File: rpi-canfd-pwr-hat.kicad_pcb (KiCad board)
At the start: 4 copper layers, 65 x 56 mm, 90 parts, among them J1 Conn_01x02, J2 Conn_01x04_Pin, J3 Raspberry_Pi, J4 Conn_01x02, J5 Conn_01x02, U1 XC6206P332MR, U10 SN74LV1T125DBV, U11 SN74LV1T125DBV, U12 SN74LV1T125DBV, U13 SN74LV1T125DBV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

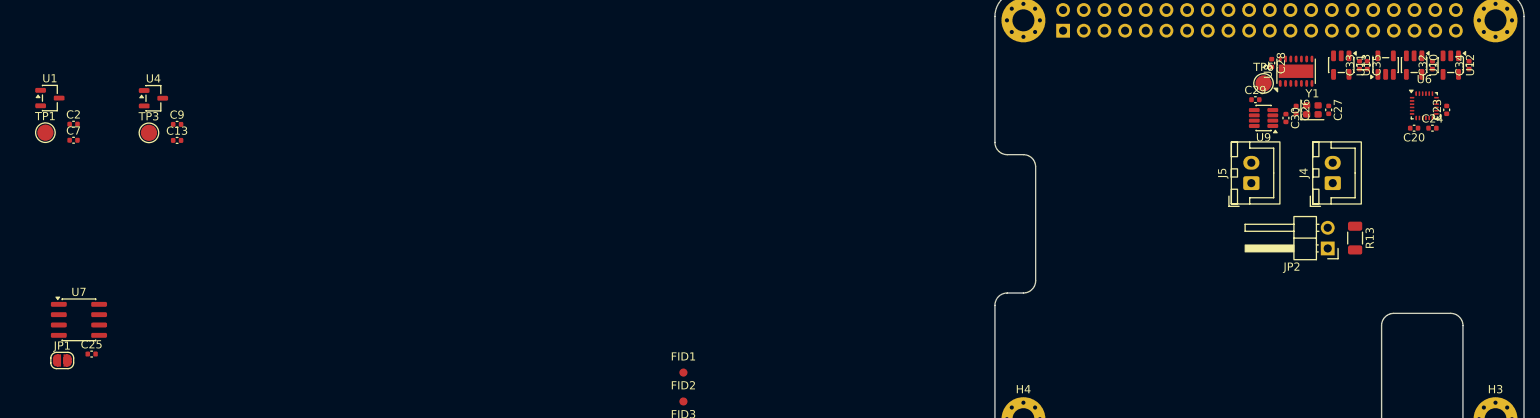
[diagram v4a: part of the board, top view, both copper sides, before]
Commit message: pcb: add eeprom routing
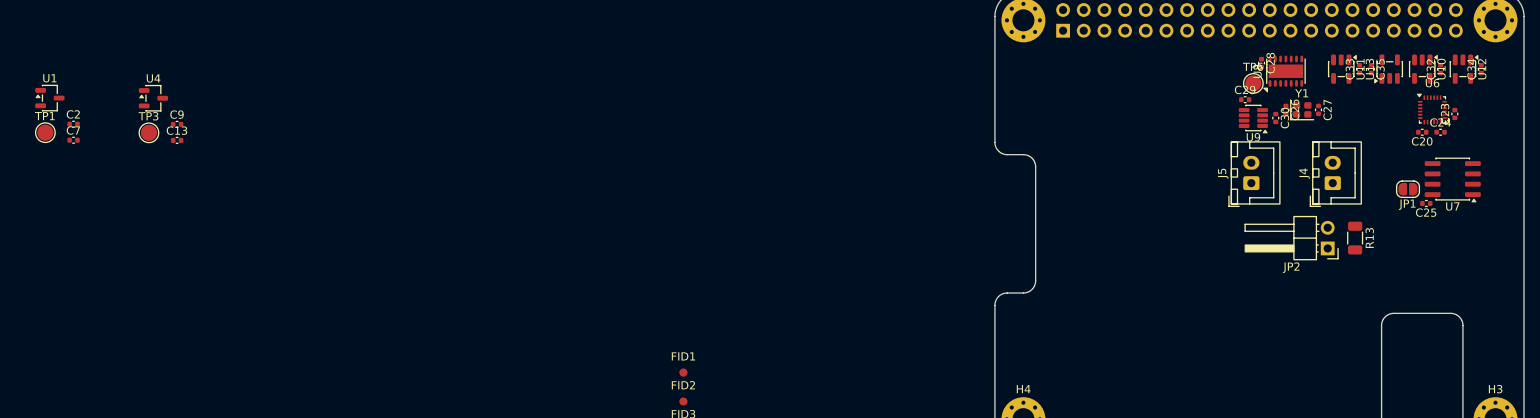
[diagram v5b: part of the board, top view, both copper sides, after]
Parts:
- moved U7 169.7 mm to (206.2, 93.0), turned to 180 degrees
- moved JP1 166.7 mm to (200.8, 94.2), turned to 180 degrees
- moved C25 165.0 mm to (203.0, 96.0), turned to 180 degrees
- moved C34 1.58 mm to (209.8, 79.5)
- moved U12 1.58 mm to (207.5, 79.5)
- moved C26 1.25 mm to (185.8, 84.5)
- moved C27 1.25 mm to (189.8, 84.5)
- moved C28 1.25 mm to (182.8, 78.8)
- moved C29 1.25 mm to (180.8, 83.2)
- moved C30 1.25 mm to (184.5, 85.5)
- moved TP6 1.25 mm to (181.8, 81.2)
- moved U8 1.25 mm to (185.8, 79.8)
- moved U9 1.25 mm to (181.8, 85.5)
- moved Y1 1.25 mm to (187.8, 84.5)
- moved C20 1.12 mm to (202.5, 87.2)
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
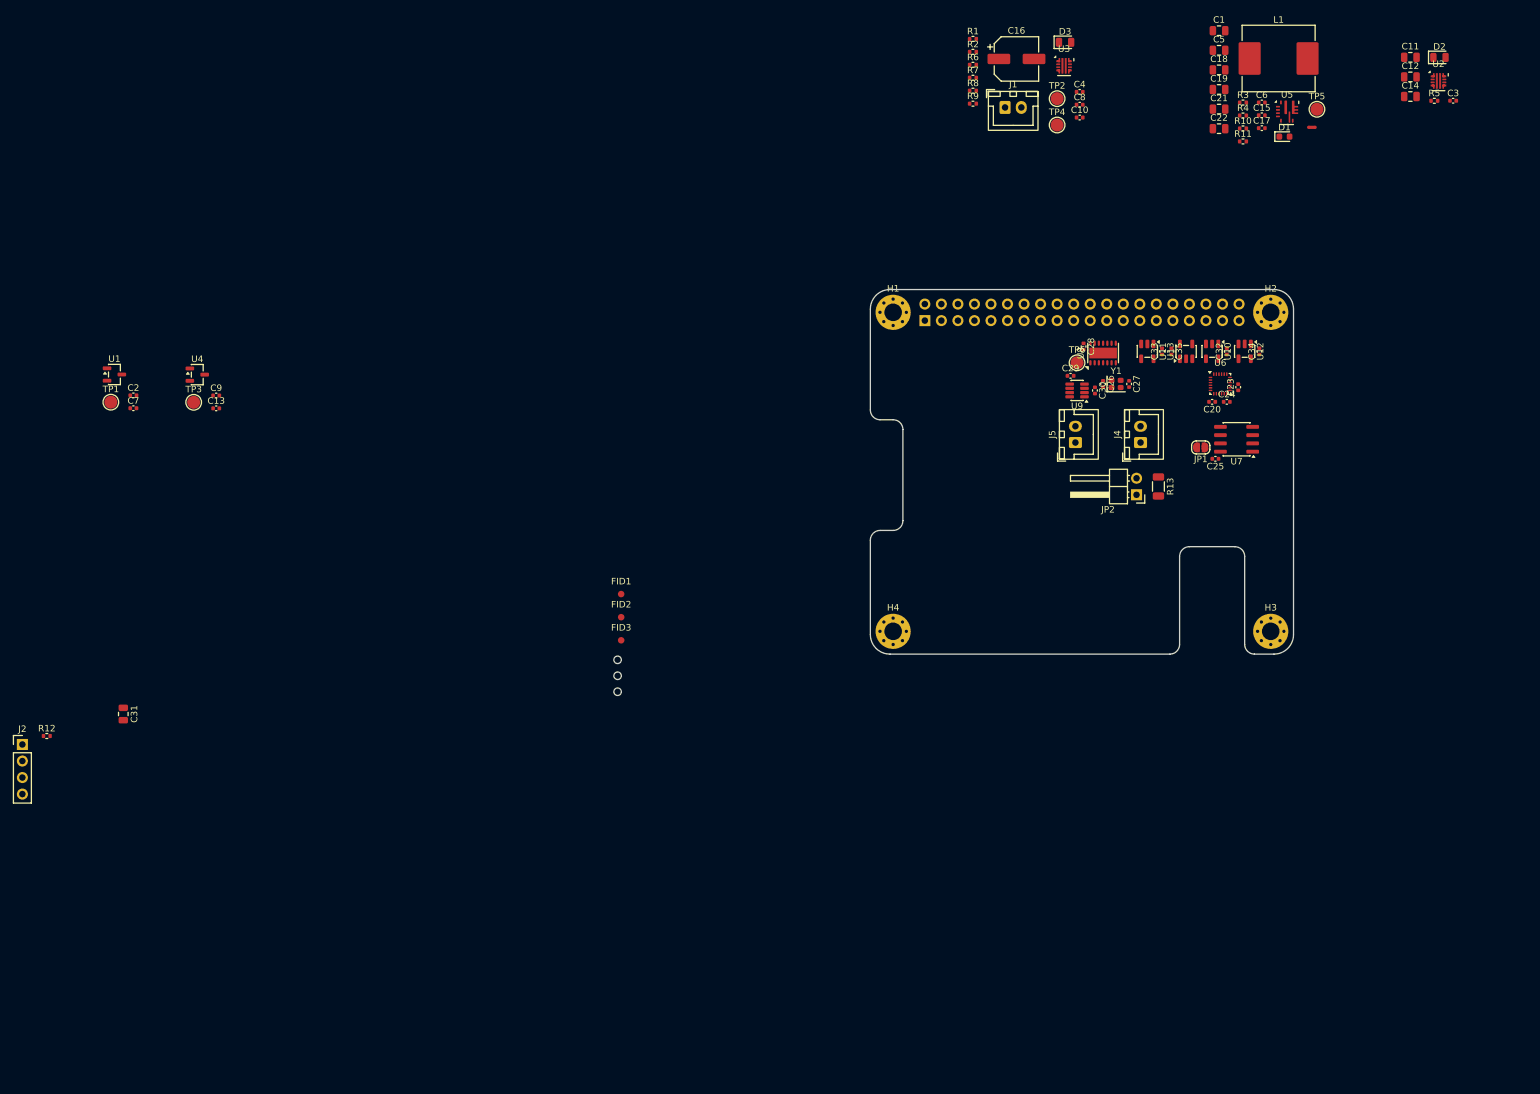
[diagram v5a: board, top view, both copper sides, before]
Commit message: pcb: add smps layout
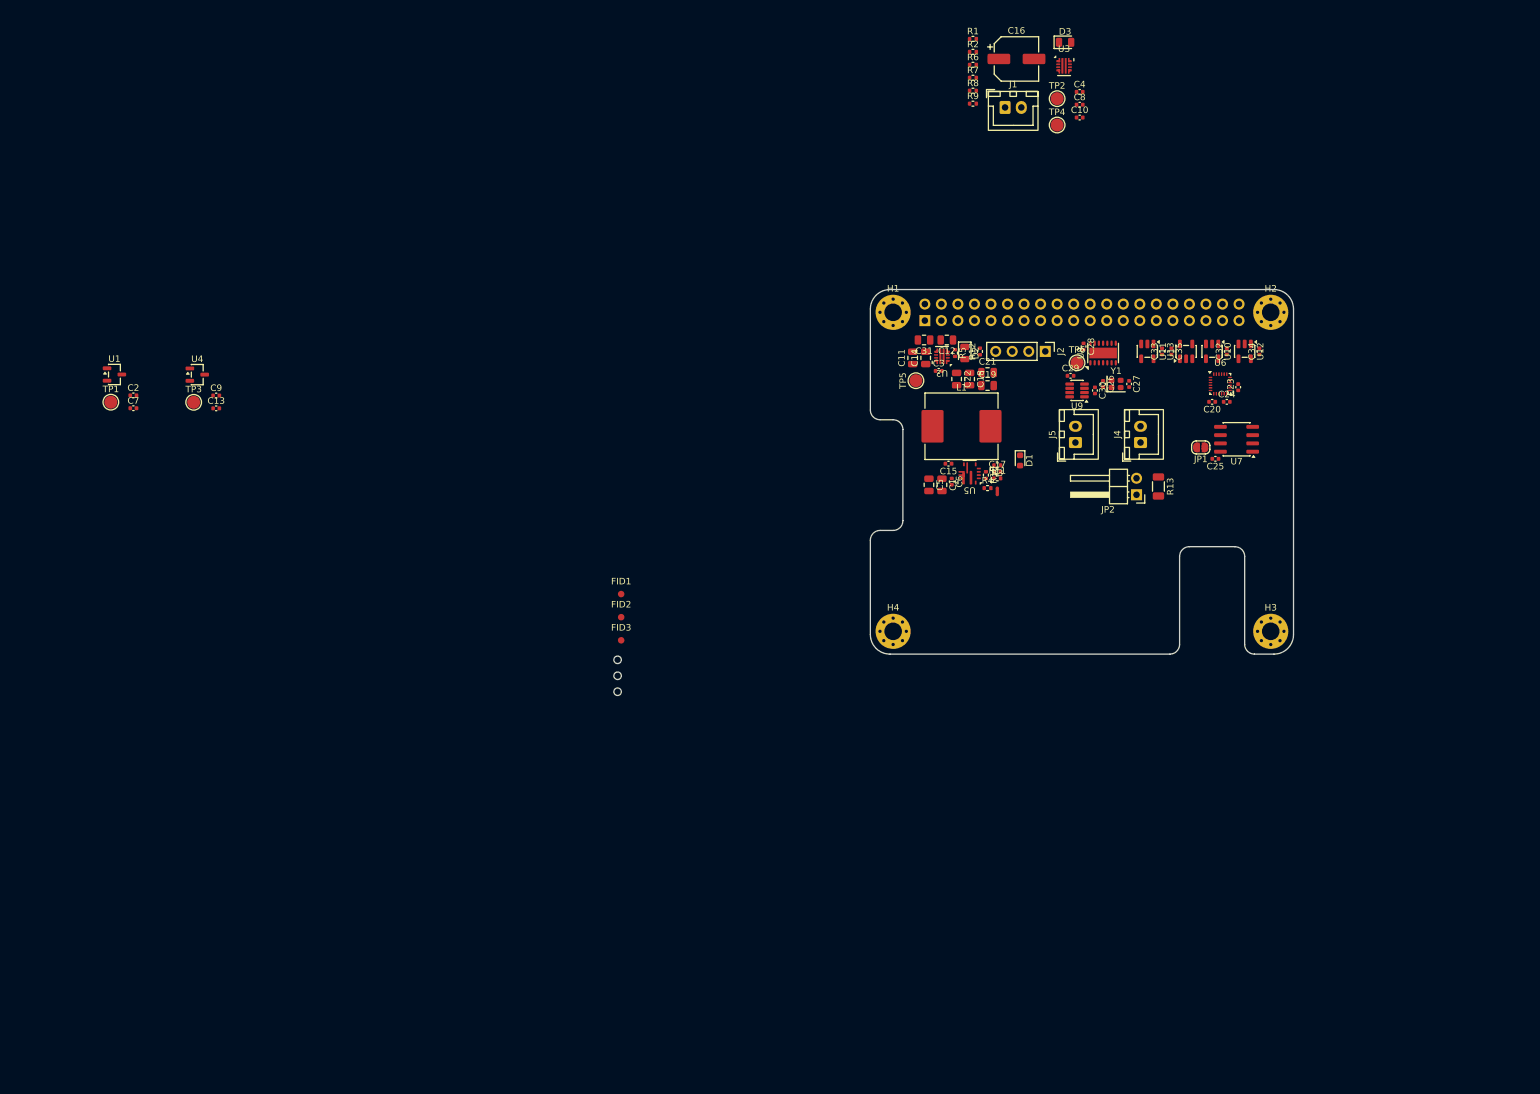
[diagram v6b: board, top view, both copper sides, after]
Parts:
- moved J2 168.3 mm to (176.9, 79.5), turned to -90 degrees
- moved R12 155.0 mm to (166.8, 79.5), turned to 90 degrees
- moved C31 135.8 mm to (158.2, 77.8), turned to 180 degrees
- moved C11 89.3 mm to (156.5, 80.5), turned to 90 degrees
- moved C3 89.3 mm to (160.5, 82.5)
- moved U2 87.2 mm to (161.0, 80.2), turned to 180 degrees
- moved D2 85.9 mm to (164.5, 79.8), turned to -90 degrees
- moved C14 84.6 mm to (158.5, 80.5), turned to 90 degrees
- moved R5 83.2 mm to (163.0, 79.8), turned to -90 degrees
- moved C12 81.9 mm to (161.8, 77.8), turned to 180 degrees
- moved C1 81.7 mm to (161.0, 100.0), turned to -90 degrees
- moved C5 80.3 mm to (159.0, 100.0), turned to -90 degrees
- moved C6 75.2 mm to (162.5, 99.5), turned to -90 degrees
- moved L1 74.6 mm to (164.0, 91.0)
- moved TP5 74.4 mm to (157.0, 84.0), turned to 90 degrees
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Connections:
- R3 pad 1: +3V3 -> +Vbuck
- R5 pad 1: +3V3 -> +5V

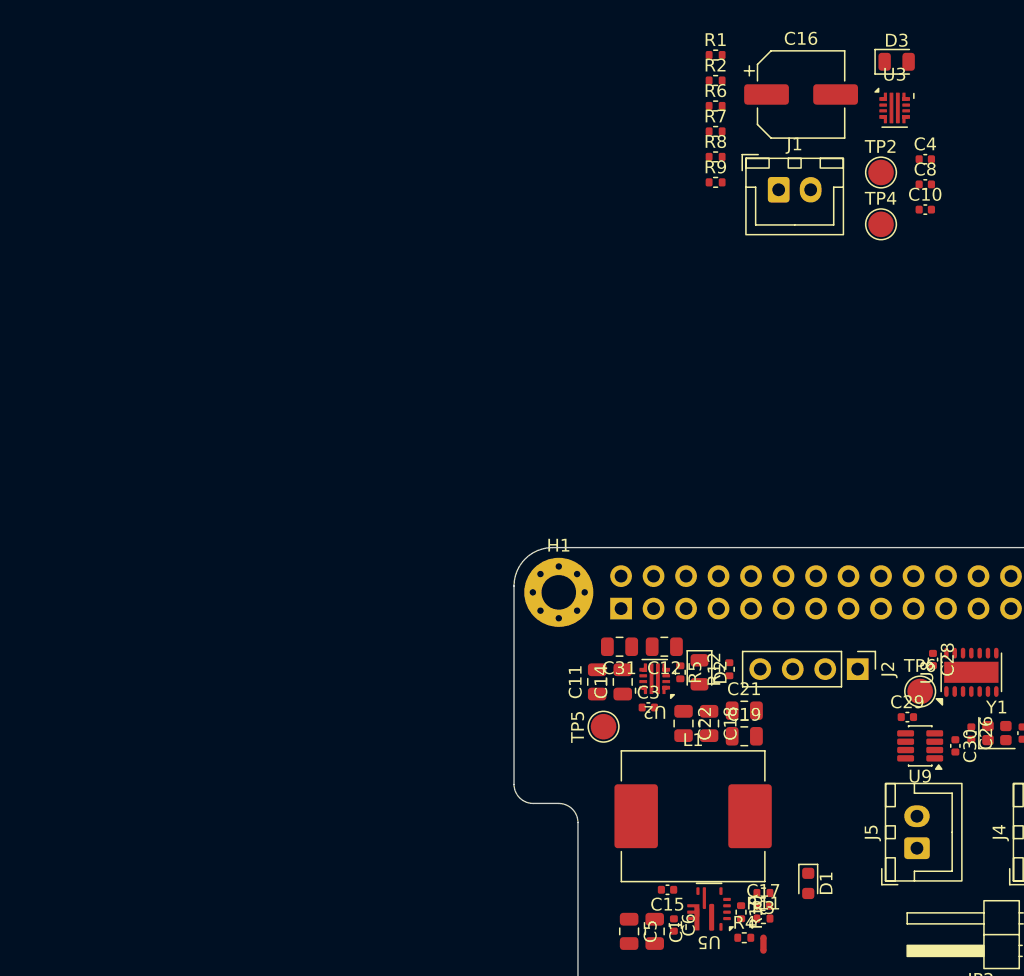
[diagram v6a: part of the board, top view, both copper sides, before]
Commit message: pcb: add smps zone
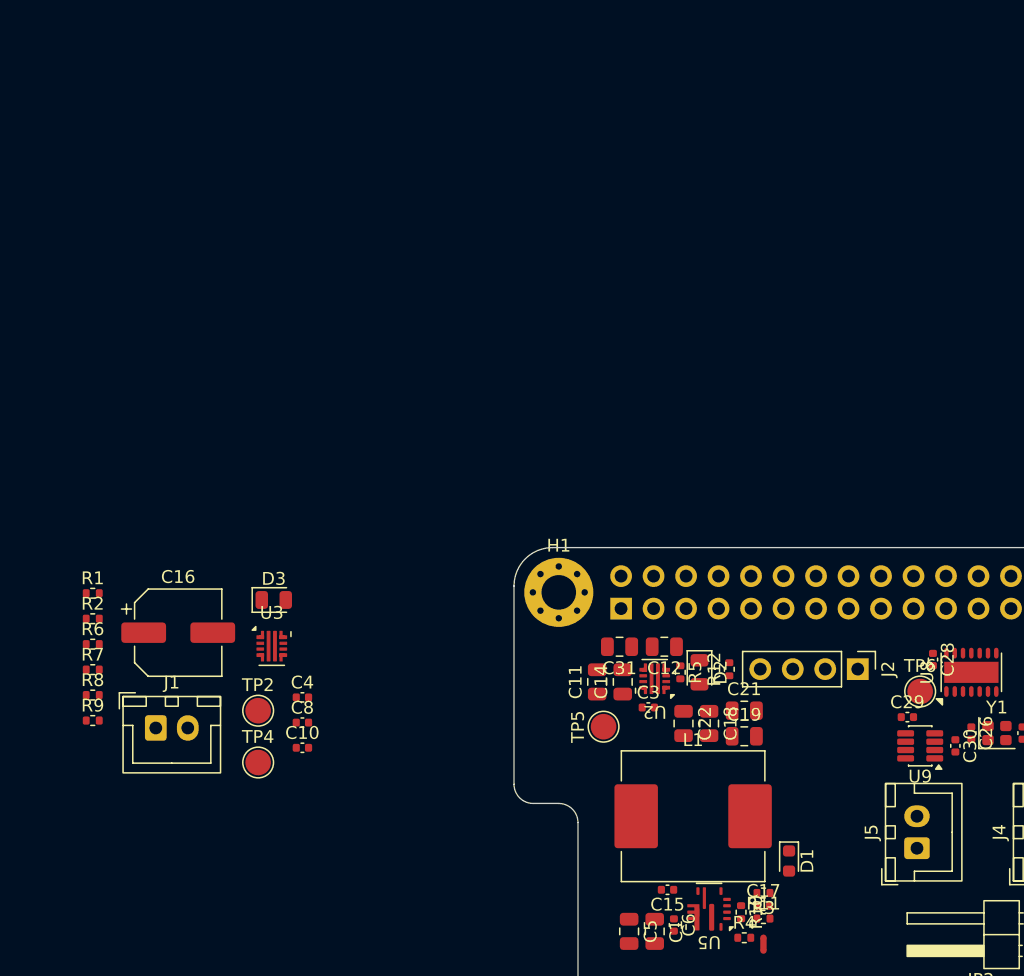
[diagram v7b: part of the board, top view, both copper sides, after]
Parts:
- moved C10 64.3 mm to (133.5, 85.7)
- moved C16 64.3 mm to (123.8, 76.7)
- moved C8 64.3 mm to (133.5, 83.7)
- moved D3 64.3 mm to (131.2, 74.1)
- moved R2 64.3 mm to (117.1, 75.6)
- moved R6 64.3 mm to (117.1, 77.5)
- moved R7 64.3 mm to (117.1, 79.5)
- moved R8 64.3 mm to (117.1, 81.5)
- moved TP2 64.3 mm to (130.0, 82.8)
- moved TP4 64.3 mm to (130.0, 86.8)
- moved U3 64.3 mm to (131.1, 77.7)
- moved C4 64.3 mm to (133.5, 81.7)
- moved J1 64.3 mm to (122.0, 84.1)
- moved R1 64.3 mm to (117.1, 73.6)
- moved R9 64.3 mm to (117.1, 83.5)
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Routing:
- added copper zone on In1.Cu, net AGND
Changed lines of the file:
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@@
 	(footprint "Capacitor_SMD:C_0402_1005Metric"
 		(layer "F.Cu")
-		(at 182.15 41.61)
+		(at 133.46 83.68)
 		(descr "Capacitor SMD 0402 (1005 Metric), square (rectangular) end terminal, IPC-7351 nominal, (Body size source: IPC-SM-782 page 76, https://www.pcb-3d.com/wordpress/wp-content/uploads/ipc-sm-782a_amendment_1_and_2.pdf)")
 		(tags "capacitor")
@@
 	(footprint "TestPoint:TestPoint_Pad_D2.0mm"
 		(layer "F.Cu")
-		(at 178.69 44.73)
+		(at 130 86.8)
 		(descr "SMD pad as test Point, diameter 2.0mm")
 		(tags "test point SMD pad")
@@
 	(footprint "Connector_JST:JST_XH_B2B-XH-A_1x02_P2.50mm_Vertical"
 		(layer "F.Cu")
-		(at 170.69 42.03)
+		(at 122 84.1)
 		(descr "JST XH series connector, B2B-XH-A (http://www.jst-mfg.com/product/pdf/eng/eXH.pdf)")
 		(tags "connector JST XH vertical")
@@
 	(footprint "Resistor_SMD:R_0402_1005Metric"
 		(layer "F.Cu")
-		(at 165.76 35.48)
+		(at 117.07 77.55)
 		(descr "Resistor SMD 0402 (1005 Metric), square (rectangular) end terminal, IPC-7351 nominal, (Body size source: IPC-SM-782 page 72, https://www.pcb-3d.com/wordpress/wp-content/uploads/ipc-sm-782a_amendment_1_and_2.pdf)")
 		(tags "resistor")
@@
 	(footprint "Resistor_SMD:R_0402_1005Metric"
 		(layer "F.Cu")
-		(at 165.76 39.46)
+		(at 117.07 81.53)
 		(descr "Resistor SMD 0402 (1005 Metric), square (rectangular) end terminal, IPC-7351 nominal, (Body size source: IPC-SM-782 page 72, https://www.pcb-3d.com/wordpress/wp-content/uploads/ipc-sm-782a_amendment_1_and_2.pdf)")
 		(tags "resistor")
@@
 	(footprint "TestPoint:TestPoint_Pad_D2.0mm"
 		(layer "F.Cu")
-		(at 178.69 40.68)
+		(at 130 82.75)
 		(descr "SMD pad as test Point, diameter 2.0mm")
 		(tags "test point SMD pad")
@@
 	(footprint "Capacitor_SMD:C_0402_1005Metric"
 		(layer "F.Cu")
-		(at 182.15 39.64)
+		(at 133.46 81.71)
 		(descr "Capacitor SMD 0402 (1005 Metric), square (rectangular) end terminal, IPC-7351 nominal, (Body size source: IPC-SM-782 page 76, https://www.pcb-3d.com/wordpress/wp-content/uploads/ipc-sm-782a_amendment_1_and_2.pdf)")
 		(tags "capacitor")
@@
 	(footprint "Capacitor_SMD:C_0402_1005Metric"
 		(layer "F.Cu")
-		(at 182.15 43.58)
+		(at 133.46 85.65)
 		(descr "Capacitor SMD 0402 (1005 Metric), square (rectangular) end terminal, IPC-7351 nominal, (Body size source: IPC-SM-782 page 76, https://www.pcb-3d.com/wordpress/wp-content/uploads/ipc-sm-782a_amendment_1_and_2.pdf)")
 		(tags "capacitor")
@@
 	(footprint "Resistor_SMD:R_0402_1005Metric"
 		(layer "F.Cu")
-		(at 165.76 33.49)
+		(at 117.07 75.56)
 		(descr "Resistor SMD 0402 (1005 Metric), square (rectangular) end terminal, IPC-7351 nominal, (Body size source: IPC-SM-782 page 72, https://www.pcb-3d.com/wordpress/wp-content/uploads/ipc-sm-782a_amendment_1_and_2.pdf)")
 		(tags "resistor")
@@
 	(footprint "LED_SMD:LED_0603_1608Metric"
 		(layer "F.Cu")
-		(at 173 96.25 -90)
+		(at 171.5 94.5 -90)
 		(descr "LED SMD 0603 (1608 Metric), square (rectangular) end terminal, IPC-7351 nominal, (Body size source: http://www.tortai-tech.com/upload/download/2011102023233369053.pdf)")
 		(tags "LED")
@@
 	(footprint "Resistor_SMD:R_0402_1005Metric"
 		(layer "F.Cu")
-		(at 165.76 37.47)
+		(at 117.07 79.54)
 		(descr "Resistor SMD 0402 (1005 Metric), square (rectangular) end terminal, IPC-7351 nominal, (Body size source: IPC-SM-782 page 72, https://www.pcb-3d.com/wordpress/wp-content/uploads/ipc-sm-782a_amendment_1_and_2.pdf)")
 		(tags "resistor")
@@
 	(footprint "LED_SMD:LED_0805_2012Metric"
 		(layer "F.Cu")
-		(at 179.91 32.025)
+		(at 131.22 74.095)
 		(descr "LED SMD 0805 (2012 Metric), square (rectangular) end terminal, IPC-7351 nominal, (Body size source: https://docs.google.com/spreadsheets/d/1BsfQQcO9C6DZCsRaXUlFlo91Tg2WpOkGARC1WS5S8t0/edit?usp=sharing)")
 		(tags "LED")
@@
 	(footprint "Resistor_SMD:R_0402_1005Metric"
 		(layer "F.Cu")
-		(at 165.76 41.45)
+		(at 117.07 83.52)
 		(descr "Resistor SMD 0402 (1005 Metric), square (rectangular) end terminal, IPC-7351 nominal, (Body size source: IPC-SM-782 page 72, https://www.pcb-3d.com/wordpress/wp-content/uploads/ipc-sm-782a_amendment_1_and_2.pdf)")
 		(tags "resistor")
@@
 	(footprint "Resistor_SMD:R_0402_1005Metric"
 		(layer "F.Cu")
-		(at 165.76 31.5)
+		(at 117.07 73.57)
 		(descr "Resistor SMD 0402 (1005 Metric), square (rectangular) end terminal, IPC-7351 nominal, (Body size source: IPC-SM-782 page 72, https://www.pcb-3d.com/wordpress/wp-content/uploads/ipc-sm-782a_amendment_1_and_2.pdf)")
 		(tags "resistor")
@@
 	(footprint "GLCS:Texas_RPW0010A_VQFN-HR-10_2x2mm_P0.5mm"
 		(layer "F.Cu")
-		(at 179.755 35.635)
+		(at 131.065 77.705)
 		(descr "VQFN-HR, 10 Pin (https://www.ti.com/lit/ds/symlink/tps56a37.pdf#page=27)")
 		(tags "VQFN-HR NO LEAD")
@@
 	(footprint "Capacitor_SMD:CP_Elec_6.3x7.7"
 		(layer "F.Cu")
-		(at 172.44 34.58)
+		(at 123.75 76.65)
 		(descr "SMD capacitor, aluminum electrolytic, Nichicon, 6.3x7.7mm")
 		(tags "capacitor electrolytic")
@@
 		(layer "Edge.Cuts")
 	)
+	(zone
+		(layer "F.Cu")
+		(hatch edge 0.5)
+		(connect_pads
+			(clearance 0)
+		)
+		(min_thickness 0.25)
+		(keepout
+			(tracks allowed)
+			(vias allowed)
+			(pads allowed)
+			(copperpour not_allowed)
+			(footprints allowed)
+		)
+		(placement
+			(enabled no)
+			(sheetname "/")
+		)
+		(fill
+			(thermal_gap 0.5)
+			(thermal_bridge_width 0.5)
+			(island_removal_mode 0)
+		)
+		(polygon
+			(pts
+				(xy 166.25 97) (xy 167 96.25) (xy 170.25 96.25) (xy 170.5 96.5) (xy 170.5 100.75) (xy 170.25 101)
+				(xy 166.5 101) (xy 166.25 100.75)
+			)
+		)
+	)
+	(zone
+		(net "AGND")
+		(layer "In1.Cu")
+		(hatch edge 0.5)
+		(connect_pads
+			(clearance 0.2)
+		)
+		(min_thickness 0.15)
+		(fill
+			(thermal_gap 0.35)
+			(thermal_bridge_width 0.35)
+			(island_removal_mode 0)
+		)
+		(polygon
+			(pts
+				(xy 166.25 97) (xy 167 96.25) (xy 170.25 96.25) (xy 170.5 96.5) (xy 170.5 100.75) (xy 170.25 101)
+				(xy 166.5 101) (xy 166.25 100.75)
+			)
+		)
+	)
 	(embedded_fonts no)
